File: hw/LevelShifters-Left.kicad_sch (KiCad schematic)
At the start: 6 parts, among them U3100 SN74LVCH16T245, U3101 SN74LVCH16T245

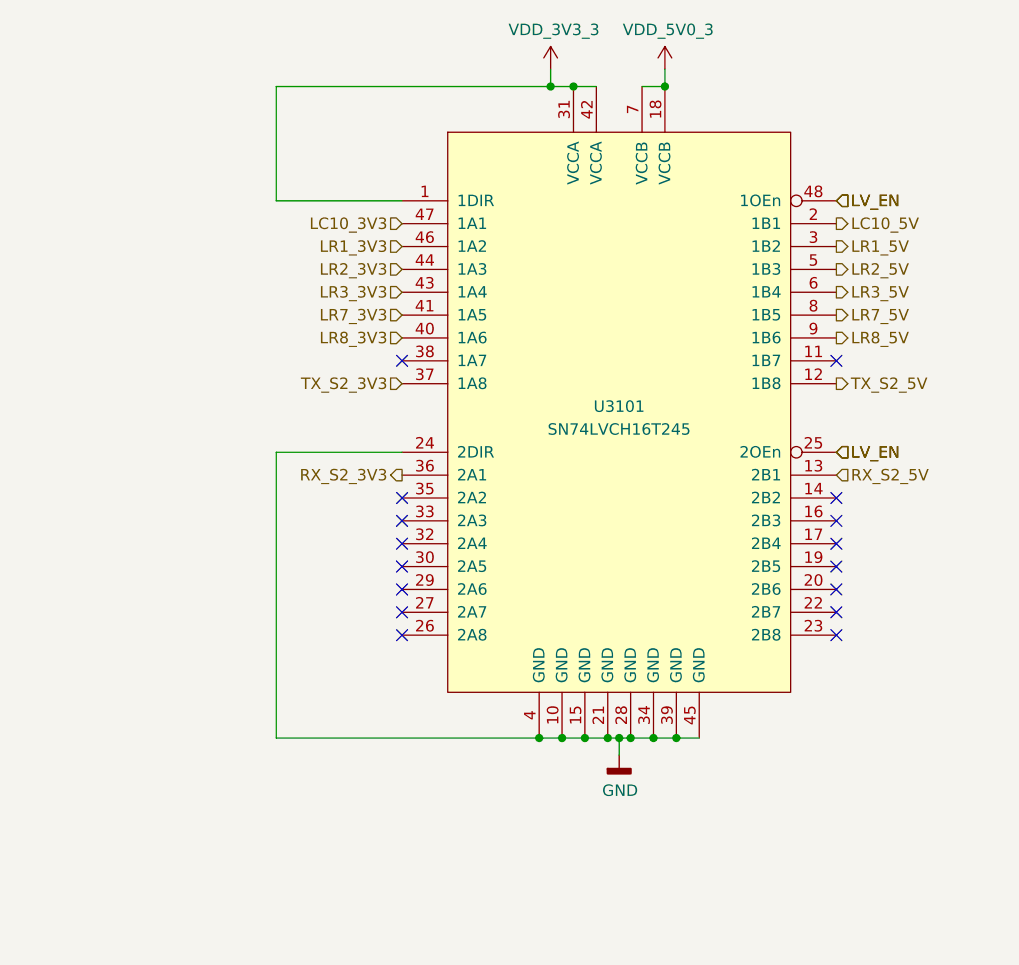
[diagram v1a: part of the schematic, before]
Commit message: Update schematic:
- Add ESD protection.
- Adjust distance bolts so they fit to the MX mounting plate.
- Make key layout symmetric.
- Add resistor to TX driver outputs.
- Use alternate IO functions on inter-board connectors.
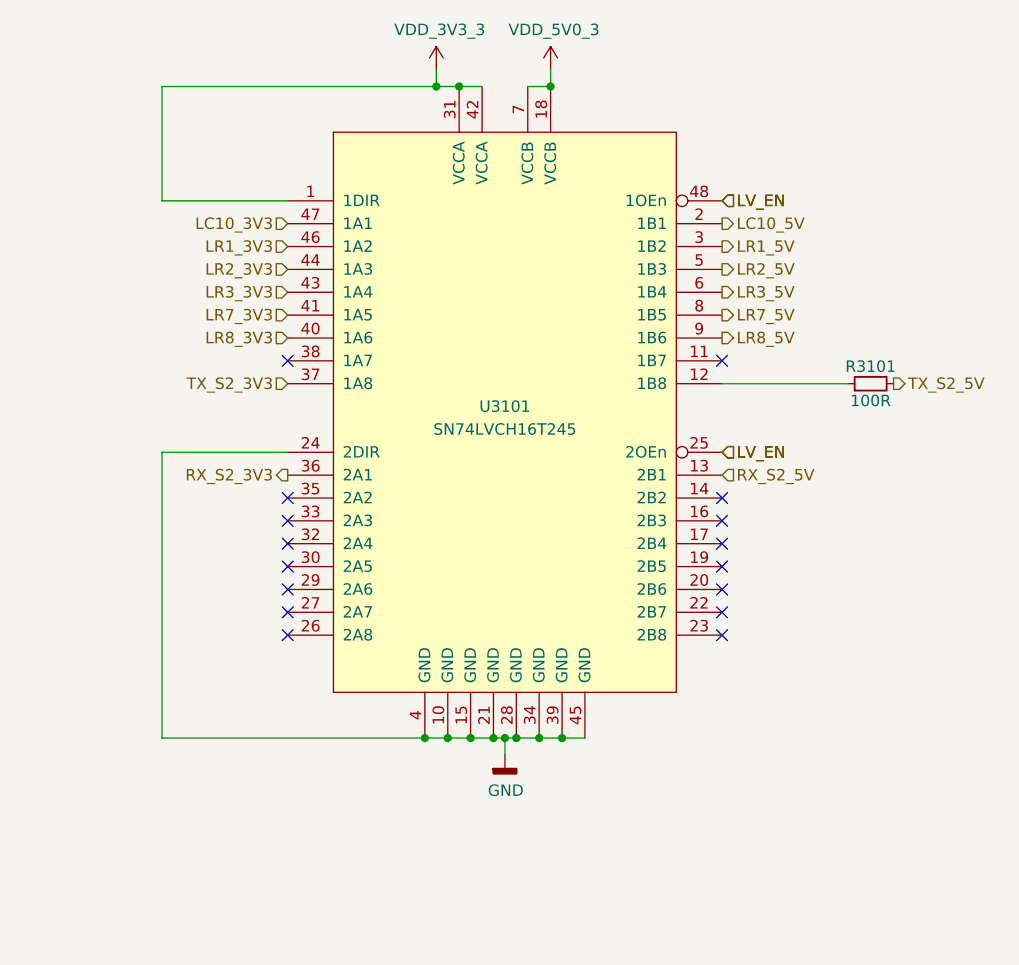
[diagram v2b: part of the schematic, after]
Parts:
- added R3101: 100R, Keyboard:R_0402, symbol Keyboard:100R
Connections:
- net TX_S2_5V: now also R3101.2; no longer U3101.12 (1B8)
- new net: R3101.1, U3101.12 (1B8)
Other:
- moved on the sheet: U3101

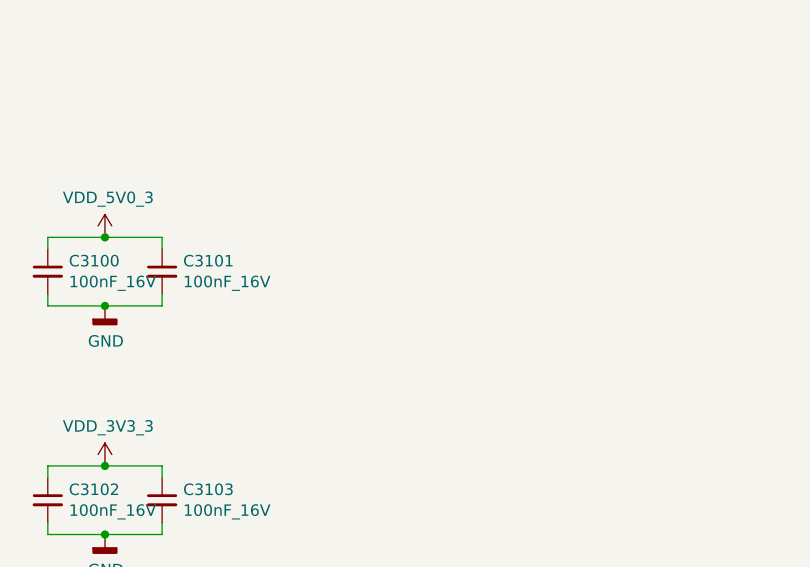
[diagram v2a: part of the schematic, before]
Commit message: Add current probes to 3.3V and pull-up to LV_EN.
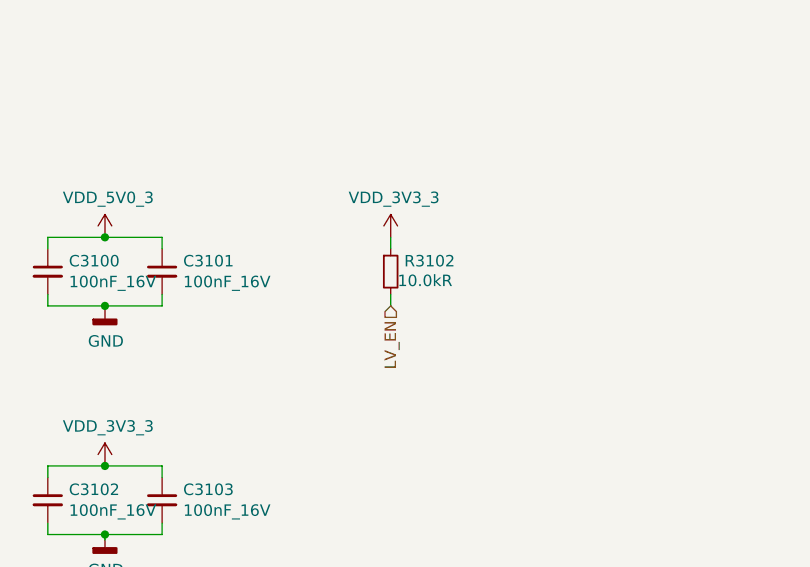
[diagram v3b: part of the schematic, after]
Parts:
- added R3102: 10.0kR, Keyboard:R_0402, symbol Keyboard:10.0kR
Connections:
- net LV_EN: now also R3102.2
- net VDD_3V3_3: now also R3102.1
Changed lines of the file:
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@@
+    (stroke (width 0) (type default) (color 0 0 0 0))
+  )
+  (wire (pts (xy 76.2 140.97) (xy 76.2 139.7))
     (stroke (width 0) (type default) (color 0 0 0 0))
   )
@@
   )
   (wire (pts (xy 38.1 139.7) (xy 44.45 139.7))
+    (stroke (width 0) (type default) (color 0 0 0 0))
+  )
+  (wire (pts (xy 76.2 146.05) (xy 76.2 147.32))
     (stroke (width 0) (type default) (color 0 0 0 0))
   )
@@
   (hierarchical_label "TX_S2_5V" (shape output) (at 265.43 59.69 0)
     (effects (font (size 1.27 1.27)) (justify left))
+  )
+  (hierarchical_label "LV_EN" (shape input) (at 76.2 147.32 270)
+    (effects (font (size 1.27 1.27)) (justify right))
   )
   (hierarchical_label "LV_EN" (shape input) (at 246.38 67.31 0)
@@
       (effects (font (size 1.524 1.524)) hide)
     )
+    (pin "1")
+    (pin "2")
+  )
+  (symbol (lib_id "Keyboard:VDD_3V3_3") (at 76.2 139.7 0) (unit 1)
+    (in_bom yes) (on_board yes)
+    (property "Reference" "#PWR03112" (id 0) (at 76.2 143.51 0)
+      (effects (font (size 1.27 1.27)) hide)
+    )
+    (property "Value" "VDD_3V3_3" (id 1) (at 76.581 135.3058 0))
+    (property "Footprint" "" (id 2) (at 76.2 139.7 0)
+      (effects (font (size 1.27 1.27)) hide)
+    )
+    (property "Datasheet" "" (id 3) (at 76.2 139.7 0)
+      (effects (font (size 1.27 1.27)) hide)
+    )
+    (pin "1")
+  )
+  (symbol (lib_id "Keyboard:10.0kR") (at 76.2 143.51 0) (unit 1)
+    (in_bom yes) (on_board yes)
+    (property "Reference" "R3102" (id 0) (at 77.6986 142.3416 0)
+      (effects (font (size 1.27 1.27)) (justify left))
+    )
+    (property "Value" "10.0kR" (id 1) (at 76.962 144.526 0)
+      (effects (font (size 1.27 1.27)) (justify left))
+    )
+    (property "Footprint" "Keyboard:R_0402" (id 2) (at 74.422 145.542 0)
+      (effects (font (size 1.27 1.27)) hide)
+    )
+    (property "Datasheet" "667-ERJ-2RKF1002X" (id 3) (at 76.962 143.002 0)
+      (effects (font (size 1.27 1.27)) hide)
+    )
+    (property "mouser#" "667-ERJ-2RKF1002X" (id 4) (at 79.502 140.462 0)
+      (effects (font (size 1.524 1.524)) hide)
+    )
